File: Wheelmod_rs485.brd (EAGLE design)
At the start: 42 x 40 mm, 52 parts, among them IC1 SN75176BPSR, SW1 RST_SW, SW2 HWB_SW, U1 ATMEGA8U2AU, U2 SI8441IS1, U3 MC33887-HSOP, U4 NFET-SOIC8, U5 LDO, X1 MINI-USB, X3 ENC, X5 LOGIC_IN, Y1 SMDRESONATOR

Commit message: Testing2
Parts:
- moved R5 8.88 mm to (8.69, 32.4), turned to 180 degrees
- moved IC1 1.46 mm to (9.70, 27.4)
- moved F1 1.13 mm to (8.94, 35.5)
- moved C15 1.01 mm to (12.5, 34.7)
- moved X2 0.68 mm to (4.25, 29.8)
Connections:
- net A: now also R5.1
- net B: now also R5.2
- net RX: no longer R5.2
- net TX: no longer R5.1
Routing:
- net B: track 7.13 -> 10.7 mm, vias 1 -> 0
- net A: track 7.13 -> 9.86 mm
- net N$22: track 4.78 -> 7.24 mm
- net DE: track 8.50 -> 7.04 mm
- net TX: track 8.39 -> 7.11 mm
- net RX: track 16.3 -> 15.3 mm
- net VCC: track 90.9 -> 91.9 mm
- net GND: vias 28 -> 27

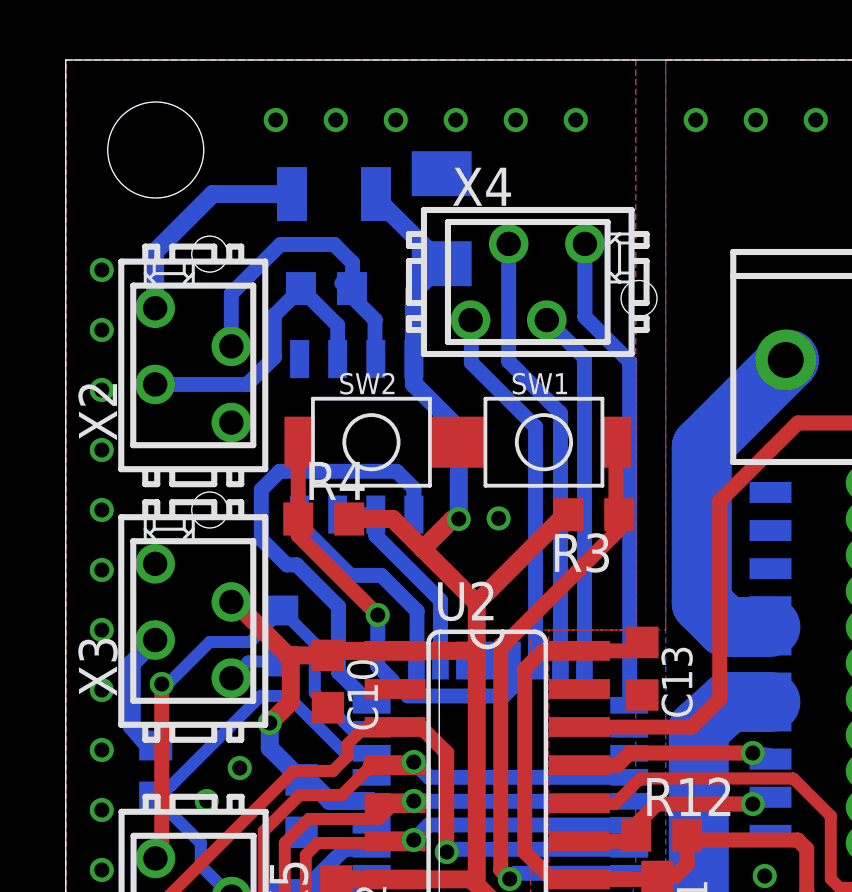
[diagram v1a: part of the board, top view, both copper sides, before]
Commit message: Final changes
Moved 2 components from bottom to top to make room for easier
installment of board.
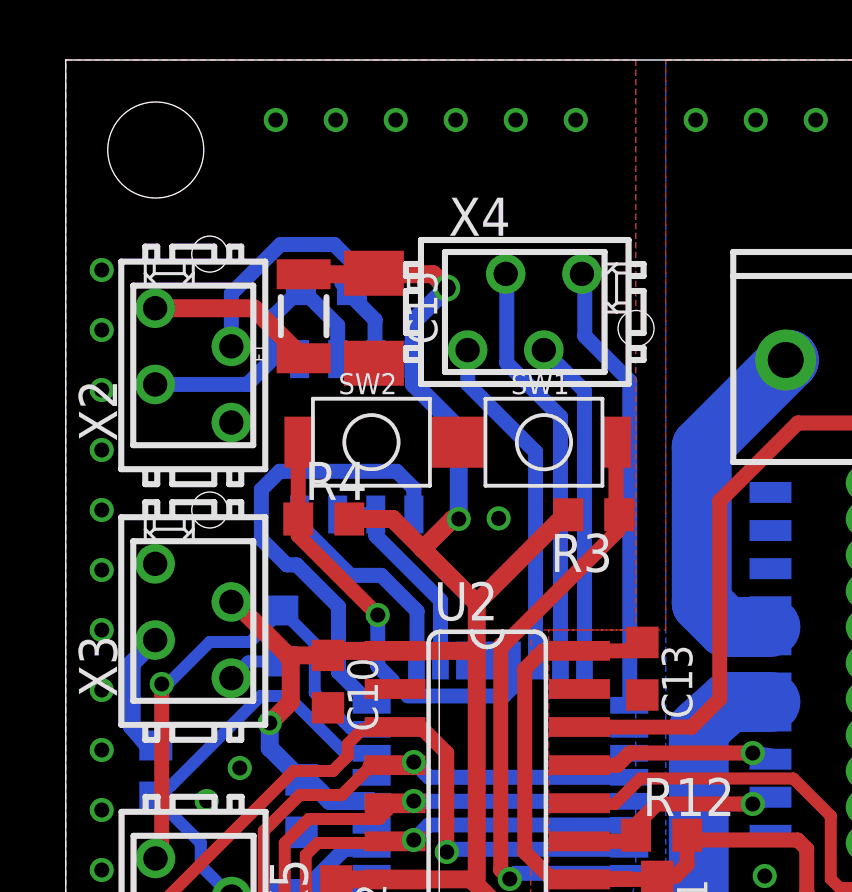
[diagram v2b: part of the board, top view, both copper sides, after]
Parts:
- moved F1 4.19 mm to (7.93, 31.5), flipped to the top, turned to 90 degrees
- moved C15 4.02 mm to (10.3, 31.4), flipped to the top, turned to 270 degrees
- moved X4 1.00 mm to (15.3, 31.6)
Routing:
- net N$22: track 7.24 -> 5.64 mm
- net VCC: track 91.9 -> 92.9 mm, vias 3 -> 4
- net N$27: track 11.9 -> 10.9 mm
- net N$24: track 12.3 -> 11.3 mm
- net N$31: track 16.0 -> 15.0 mm
- net N$26: track 14.6 -> 13.6 mm
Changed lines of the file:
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@@
 </polygon>
 <hole x="4.8" y="33.53" drill="1.2"/>
-<hole x="19.11" y="32.05" drill="1.2"/>
+<hole x="19.01" y="31.05" drill="1.2"/>
 <text x="7.27" y="36.91" size="1.778" layer="48" rot="R270">RS485</text>
 <text x="12.53" y="35.22" size="1.778" layer="48">GPIO</text>
@@
 <attribute name="OC_FARNELL" value="3784629" x="4.25" y="29.82" size="1.778" layer="27" rot="R90" display="off"/>
 </element>
-<element name="F1" library="SparkFun" package="PTC-1206" value="100mA" x="8.94" y="35.53" rot="MR180"/>
-<element name="C15" library="rcl" package="C1206K" value="10uF" x="12.53" y="34.71" rot="MR90"/>
-<element name="X4" library="con-amp-micromatch" package="MICROMATCH-4" value="" x="15.4" y="32.6">
-<attribute name="OC_NEWARK" value="19R8124" x="15.4" y="32.6" size="1.778" layer="27" display="off"/>
-<attribute name="MPN" value="7-215464-4" x="15.4" y="32.6" size="1.778" layer="27" display="off"/>
-<attribute name="MF" value="" x="15.4" y="32.6" size="1.778" layer="27" display="off"/>
-<attribute name="OC_FARNELL" value="3784629" x="15.4" y="32.6" size="1.778" layer="27" display="off"/>
+<element name="F1" library="SparkFun" package="PTC-1206" value="100mA" x="7.93" y="31.46" rot="R90"/>
+<element name="C15" library="rcl" package="C1206K" value="10uF" x="10.27" y="31.39" rot="R270"/>
+<element name="X4" library="con-amp-micromatch" package="MICROMATCH-4" value="" x="15.3" y="31.6">
+<attribute name="OC_NEWARK" value="19R8124" x="15.3" y="31.6" size="1.778" layer="27" display="off"/>
+<attribute name="MPN" value="7-215464-4" x="15.3" y="31.6" size="1.778" layer="27" display="off"/>
+<attribute name="MF" value="" x="15.3" y="31.6" size="1.778" layer="27" display="off"/>
+<attribute name="OC_FARNELL" value="3784629" x="15.3" y="31.6" size="1.778" layer="27" display="off"/>
 </element>
 </elements>
@@
 <wire x1="13.1" y1="24.7" x2="12.9" y2="24.7" width="0.6" layer="1"/>
 <wire x1="12.9" y1="24.7" x2="11.9" y2="23.7" width="0.6" layer="1"/>
-<wire x1="11.605" y1="30.0308" x2="11.605" y2="32.285" width="0.6" layer="16"/>
-<wire x1="11.605" y1="32.285" x2="12.53" y2="33.21" width="0.6" layer="16"/>
-<wire x1="10.34" y1="35.53" x2="10.34" y2="35.4" width="0.6" layer="16"/>
-<wire x1="10.34" y1="35.4" x2="12.53" y2="33.21" width="0.6" layer="16"/>
+<wire x1="7.93" y1="32.86" x2="10.24" y2="32.86" width="0.6" layer="1"/>
+<wire x1="10.24" y1="32.86" x2="10.27" y2="32.89" width="0.6" layer="1"/>
+<wire x1="10.24" y1="32.86" x2="12.24" y2="32.86" width="0.6" layer="1"/>
+<wire x1="12.24" y1="32.86" x2="12.7" y2="32.4" width="0.6" layer="1"/>
+<via x="12.7" y="32.4" extent="1-16" drill="0.6"/>
+<wire x1="12.7" y1="32.4" x2="11.6" y2="31.3" width="0.6" layer="16"/>
+<wire x1="11.6" y1="31.3" x2="11.6" y2="30.0358" width="0.6" layer="16"/>
+<wire x1="11.6" y1="30.0358" x2="11.605" y2="30.0308" width="0.6" layer="16"/>
 </signal>
 <signal name="N$8">
@@
 <contactref element="X2" pad="1"/>
 <contactref element="F1" pad="1"/>
-<wire x1="2.98" y1="31.725" x2="2.98" y2="33.61" width="0.6" layer="16"/>
-<wire x1="2.98" y1="33.61" x2="4.9" y2="35.53" width="0.6" layer="16"/>
-<wire x1="4.9" y1="35.53" x2="7.54" y2="35.53" width="0.6" layer="16"/>
+<wire x1="2.98" y1="31.725" x2="6.265" y2="31.725" width="0.6" layer="1"/>
+<wire x1="6.265" y1="31.725" x2="7.93" y2="30.06" width="0.6" layer="1"/>
 </signal>
 <signal name="B">
@@
 <contactref element="X4" pad="4"/>
 <wire x1="15.66" y1="20.0126" x2="15.69" y2="19.9826" width="0.5" layer="16"/>
-<wire x1="15.66" y1="20.0126" x2="15.66" y2="27.77" width="0.5" layer="16"/>
-<wire x1="15.66" y1="27.77" x2="13.52" y2="29.91" width="0.5" layer="16"/>
-<wire x1="13.52" y1="29.91" x2="13.52" y2="31.305" width="0.5" layer="16"/>
-<wire x1="13.52" y1="31.305" x2="13.495" y2="31.33" width="0.5" layer="16"/>
+<wire x1="15.66" y1="20.0126" x2="15.66" y2="26.94" width="0.5" layer="16"/>
+<wire x1="15.66" y1="26.94" x2="13.4" y2="29.2" width="0.5" layer="16"/>
+<wire x1="13.4" y1="29.2" x2="13.4" y2="30.325" width="0.5" layer="16"/>
+<wire x1="13.4" y1="30.325" x2="13.395" y2="30.33" width="0.5" layer="16"/>
 </signal>
 <signal name="N$26">
 <contactref element="U1" pad="15"/>
 <contactref element="X4" pad="3"/>
-<wire x1="14.765" y1="33.87" x2="14.765" y2="29.955" width="0.5" layer="16"/>
-<wire x1="14.765" y1="29.955" x2="16.49" y2="28.23" width="0.5" layer="16"/>
-<wire x1="16.49" y1="28.23" x2="16.49" y2="19.9826" width="0.5" layer="16"/>
+<wire x1="14.7" y1="29.9" x2="14.7" y2="32.835" width="0.5" layer="16"/>
+<wire x1="14.7" y1="32.835" x2="14.665" y2="32.87" width="0.5" layer="16"/>
+<wire x1="16.49" y1="19.9826" x2="16.49" y2="28.11" width="0.5" layer="16"/>
+<wire x1="16.49" y1="28.11" x2="14.7" y2="29.9" width="0.5" layer="16"/>
 </signal>
 <signal name="N$27">
 <contactref element="U1" pad="16"/>
 <contactref element="X4" pad="2"/>
-<wire x1="17.29" y1="19.9826" x2="17.29" y2="30.075" width="0.5" layer="16"/>
-<wire x1="17.29" y1="30.075" x2="16.035" y2="31.33" width="0.5" layer="16"/>
+<wire x1="17.29" y1="19.9826" x2="17.29" y2="28.975" width="0.5" layer="16"/>
+<wire x1="17.29" y1="28.975" x2="15.935" y2="30.33" width="0.5" layer="16"/>
 </signal>
 <signal name="N$31">
 <contactref element="U1" pad="17"/>
 <contactref element="X4" pad="1"/>
-<wire x1="17.305" y1="33.87" x2="17.305" y2="31.435" width="0.5" layer="16"/>
-<wire x1="17.305" y1="31.435" x2="18.8" y2="29.94" width="0.5" layer="16"/>
-<wire x1="18.8" y1="29.94" x2="18.8" y2="18.5074" width="0.5" layer="16"/>
 <wire x1="18.8" y1="18.5074" x2="18.7826" y2="18.49" width="0.5" layer="16"/>
+<wire x1="18.8" y1="18.5074" x2="18.8" y2="29.3" width="0.5" layer="16"/>
+<wire x1="18.8" y1="29.3" x2="17.3" y2="30.8" width="0.5" layer="16"/>
+<wire x1="17.3" y1="30.8" x2="17.3" y2="32.775" width="0.5" layer="16"/>
+<wire x1="17.3" y1="32.775" x2="17.205" y2="32.87" width="0.5" layer="16"/>
 </signal>
 </signals>
